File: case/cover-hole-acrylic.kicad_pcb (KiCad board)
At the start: 2 copper layers, 20.5 x 58.5 mm, 4 parts

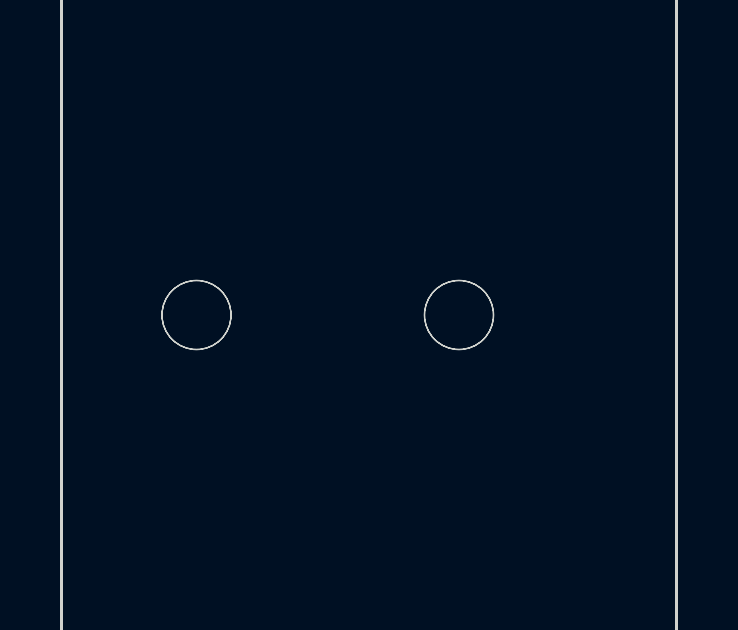
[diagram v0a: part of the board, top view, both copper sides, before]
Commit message: fix dxf files
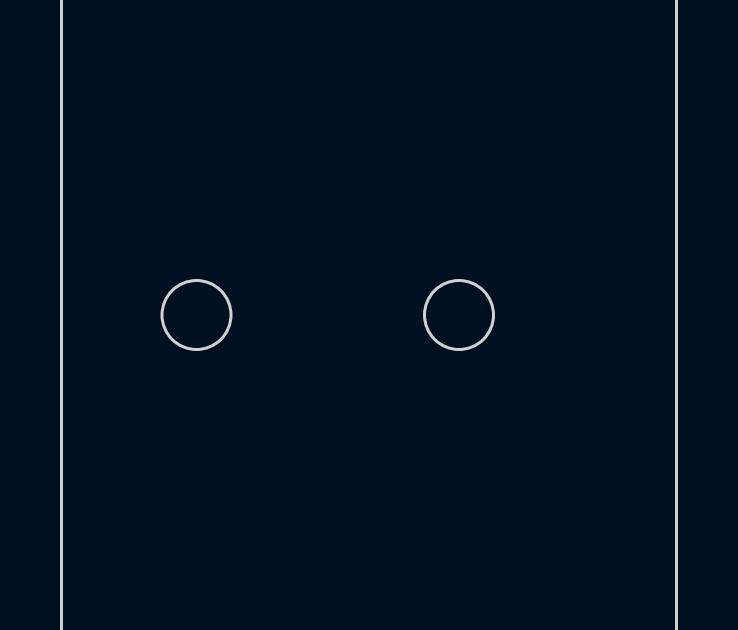
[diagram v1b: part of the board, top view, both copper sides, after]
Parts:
- removed the H6 at (130.0, 84.0)
- removed the H7 at (138.8, 84.0)
- H6, H7: footprint kbd:thread_m2 -> pica:thread_m2_hole
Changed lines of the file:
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@@
     (pad_to_mask_clearance 0)
     (pcbplotparams
-      (layerselection 0x0000080_7ffffffe)
+      (layerselection 0x0001000_7ffffffe)
       (disableapertmacros false)
       (usegerberextensions true)
@@
       (svguseinch false)
       (svgprecision 6)
-      (excludeedgelayer false)
+      (excludeedgelayer true)
       (plotframeref false)
       (viasonmask false)
@@
       (hpglpenspeed 20)
       (hpglpendiameter 15.000000)
-      (dxfpolygonmode true)
+      (dxfpolygonmode false)
       (dxfimperialunits false)
       (dxfusepcbnewfont true)
@@
   )
   (net 0 "")
-  (footprint "kbd:thread_m2" (layer "F.Cu")
+  (footprint "pica:thread_m2_hole" (layer "F.Cu")
     (at 138.75 84)
     (descr "Mounting Hole 2.2mm, no annular, M2")
     (tags "mounting hole 2.2mm no annular m2")
-    (property "Sheetfile" "left.kicad_sch")
+    (property "Sheetfile" "full.kicad_sch")
     (property "Sheetname" "")
-    (attr exclude_from_pos_files)
+    (attr exclude_from_pos_files exclude_from_bom)
     (fp_text reference "H7" (at -0.95 -0.55) (layer "F.Fab") hide
       (effects (font (size 1 1) (thickness 0.15)))
@@
       (effects (font (size 1 1) (thickness 0.15)))
     )
-    (pad "" np_thru_hole circle locked (at 0 0) (size 2.3 2.3) (drill 2.3) (layers *.Cu *.Mask))
+    (fp_circle (center 0 0) (end 1.15 0) (layer "Edge.Cuts") (width 0.1) (fill none))
   )
-  (footprint "kbd:thread_m2" (layer "F.Cu")
+  (footprint "pica:thread_m2_hole" (layer "F.Cu")
     (at 130 84)
     (descr "Mounting Hole 2.2mm, no annular, M2")
     (tags "mounting hole 2.2mm no annular m2")
-    (property "Sheetfile" "full.kicad_sch")
+    (property "Sheetfile" "left.kicad_sch")
     (property "Sheetname" "")
-    (attr exclude_from_pos_files)
+    (attr exclude_from_pos_files exclude_from_bom)
     (fp_text reference "H6" (at -0.95 -0.55) (layer "F.Fab") hide
       (effects (font (size 1 1) (thickness 0.15)))
@@
       (effects (font (size 1 1) (thickness 0.15)))
     )
-    (pad "" np_thru_hole circle locked (at 0 0) (size 2.3 2.3) (drill 2.3) (layers *.Cu *.Mask))
-  )
-  (footprint "kbd:thread_m2" (layer "F.Cu")
-    (at 138.75 84)
-    (descr "Mounting Hole 2.2mm, no annular, M2")
-    (tags "mounting hole 2.2mm no annular m2")
-    (property "Sheetfile" "full.kicad_sch")
-    (property "Sheetname" "")
-    (attr exclude_from_pos_files)
-    (fp_text reference "H7" (at -0.95 -0.55) (layer "F.Fab") hide
-      (effects (font (size 1 1) (thickness 0.15)))
-    )
-    (fp_text value "MountingHole" (at 0 0.55) (layer "F.Fab") hide
-      (effects (font (size 1 1) (thickness 0.15)))
-    )
-    (pad "" np_thru_hole circle locked (at 0 0) (size 2.3 2.3) (drill 2.3) (layers *.Cu *.Mask))
-  )
-  (footprint "kbd:thread_m2" (layer "F.Cu")
-    (at 130 84)
-    (descr "Mounting Hole 2.2mm, no annular, M2")
-    (tags "mounting hole 2.2mm no annular m2")
-    (property "Sheetfile" "left.kicad_sch")
-    (property "Sheetname" "")
-    (attr exclude_from_pos_files)
-    (fp_text reference "H6" (at -0.95 -0.55) (layer "F.Fab") hide
-      (effects (font (size 1 1) (thickness 0.15)))
-    )
-    (fp_text value "MountingHole" (at 0 0.55) (layer "F.Fab") hide
-      (effects (font (size 1 1) (thickness 0.15)))
-    )
-    (pad "" np_thru_hole circle locked (at 0 0) (size 2.3 2.3) (drill 2.3) (layers *.Cu *.Mask))
+    (fp_circle (center 0 0) (end 1.15 0) (layer "Edge.Cuts") (width 0.1) (fill none))
   )
   (gr_arc (start 146 117) (mid 145.251221 118.302195) (end 143.75 118.25) (layer "Edge.Cuts") (width 0.1))
